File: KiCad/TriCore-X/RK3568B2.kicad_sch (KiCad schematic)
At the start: 1 part, among them U1 RK3568B2

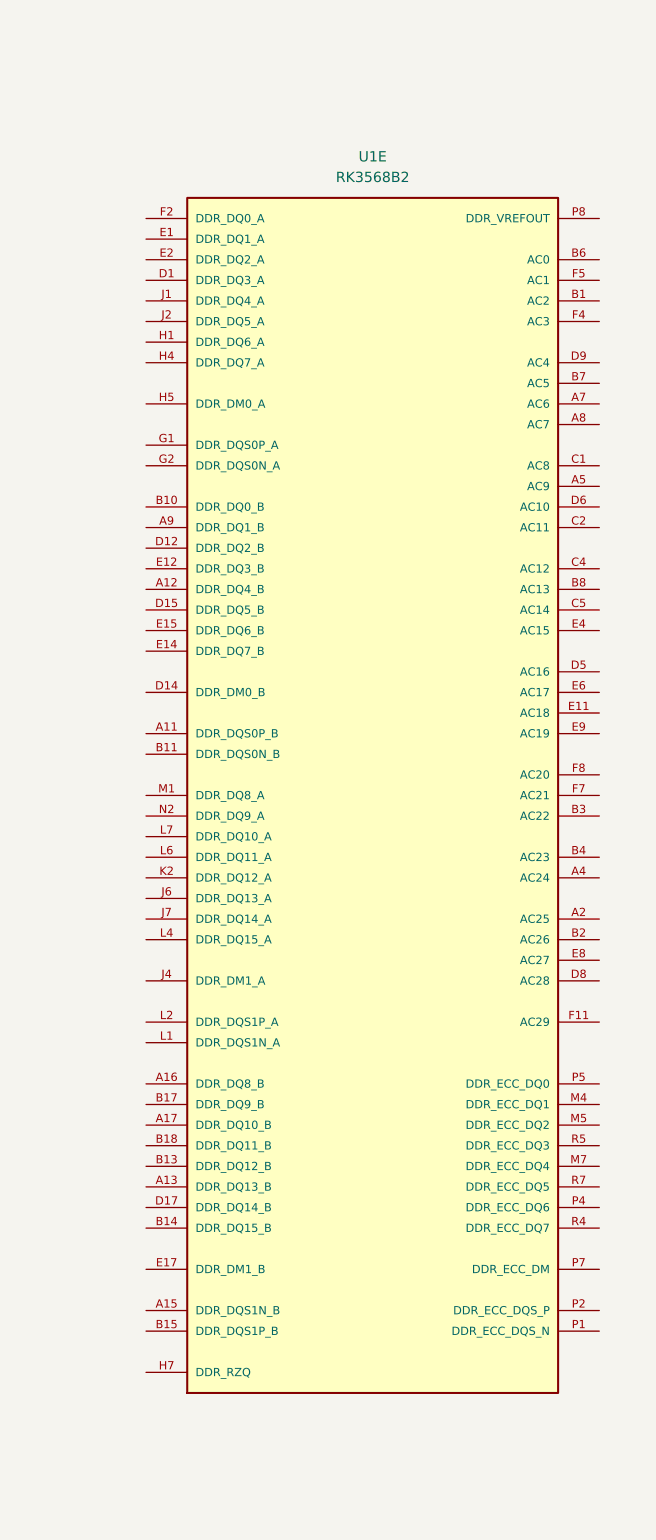
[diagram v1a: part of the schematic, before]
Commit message: feat : add some Expansion Ports (work in progress)
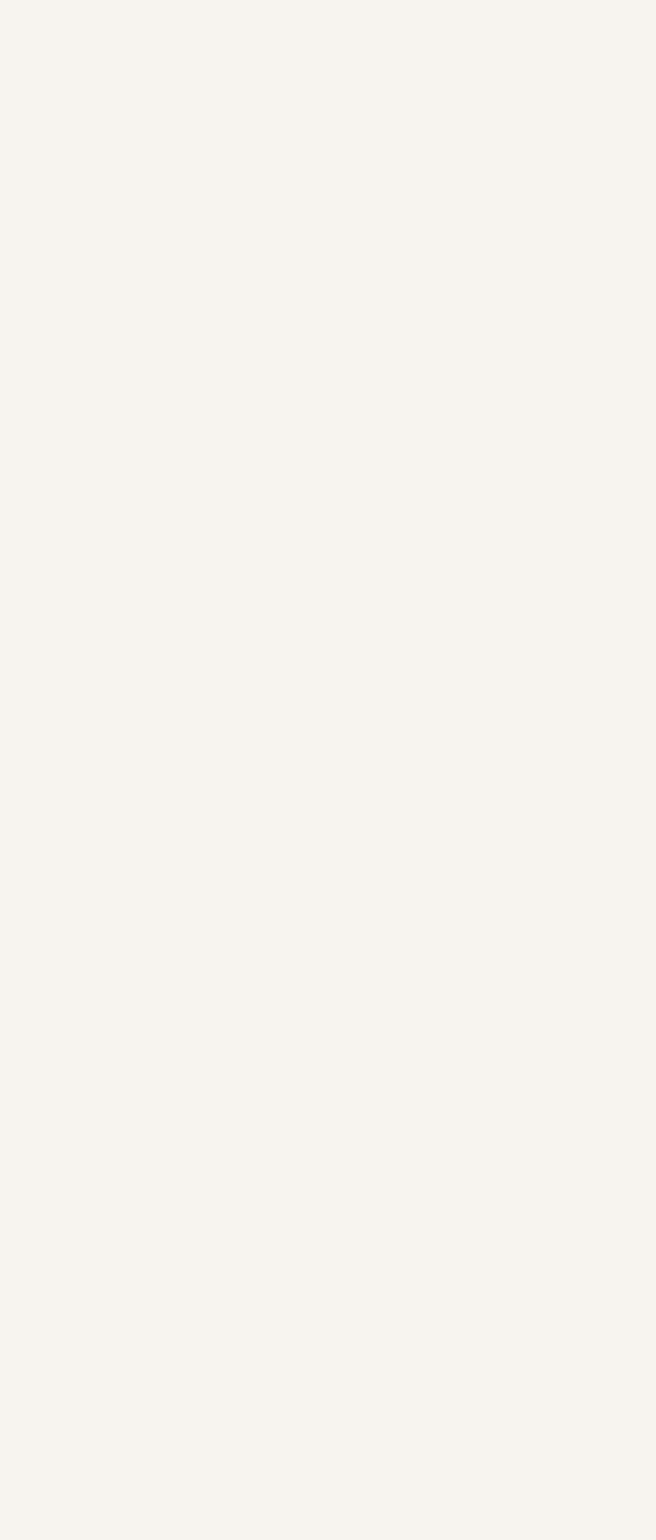
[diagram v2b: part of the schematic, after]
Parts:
- removed unit 5 of U1

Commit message: refactor: change core MCU to STM32H723 and add LPDDR4/HDMI support
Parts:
- removed unit 16 of U1
- added WIFI1: BL-M8822CU3-A, BL-M8822CU3-A:WIRELM-SMD_BL-M8822CU3-A, symbol BL-M8822CU3-A:BL-M8822CU3-A
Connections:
- net AVSS1: now also WIFI1.11 (GND), WIFI1.13 (GND), WIFI1.18 (GND), WIFI1.20 (GND), WIFI1.21 (GND), WIFI1.23 (GND), WIFI1.24 (GND), WIFI1.25 (GND), WIFI1.29 (GND), WIFI1.32 (GND), WIFI1.5 (GND), WIFI1.8 (GND)
- no-connect marks 0 -> 6

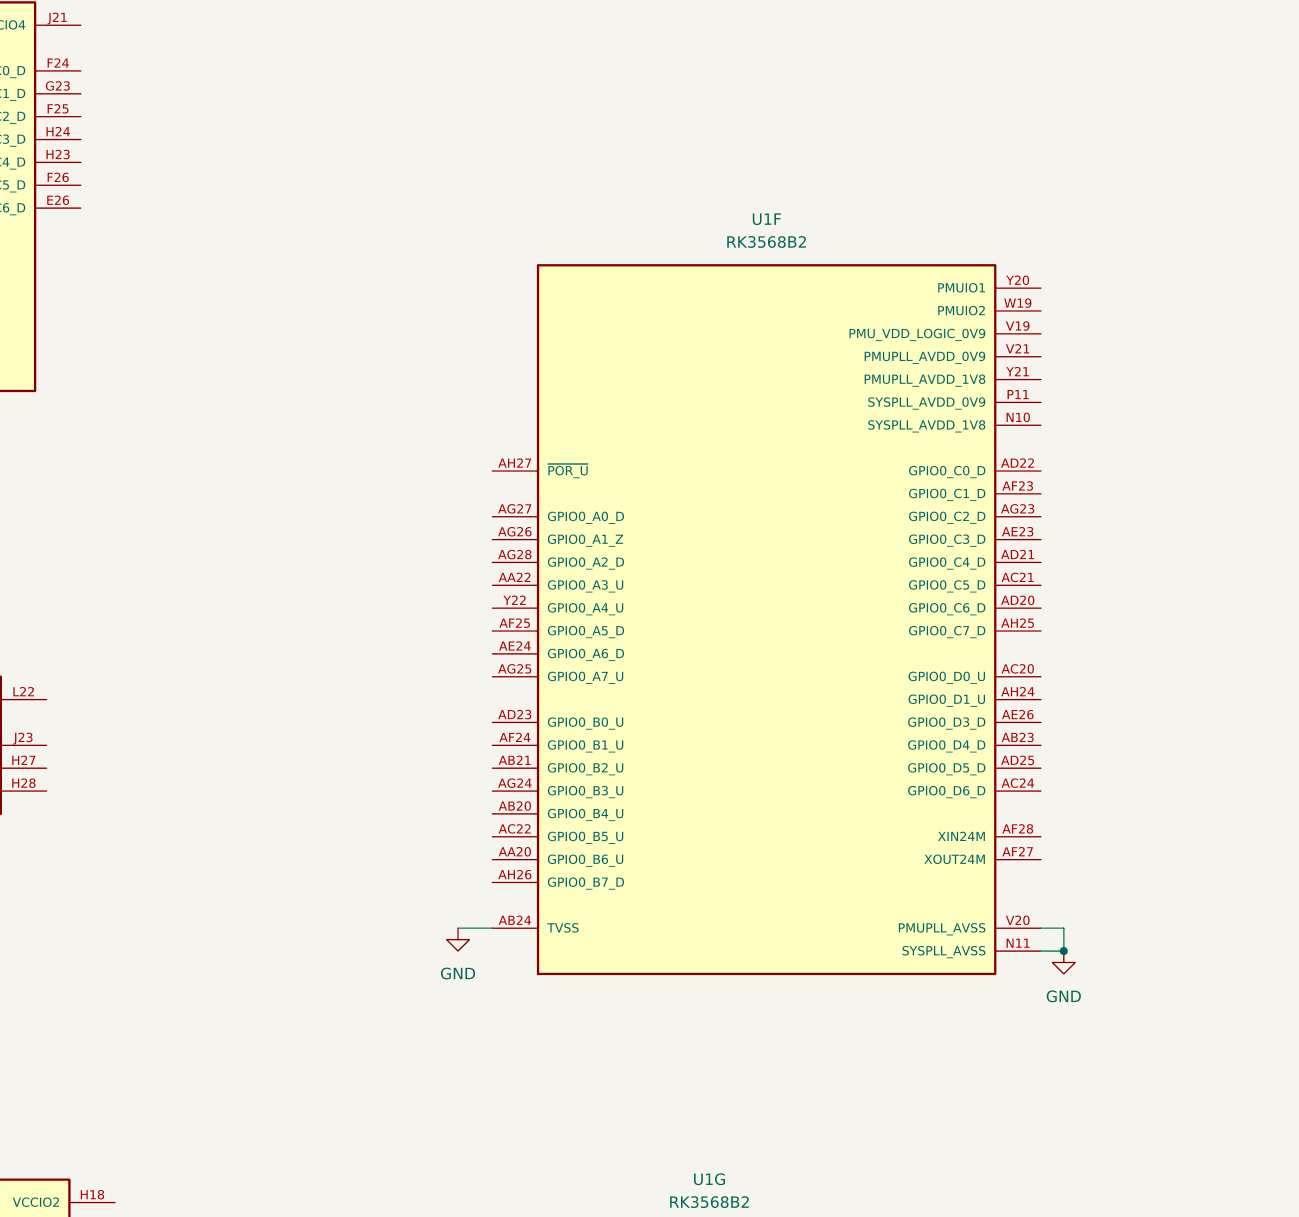
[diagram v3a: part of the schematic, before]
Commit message: feat: complete schematic for RK809-5 PMIC peripheral circuits
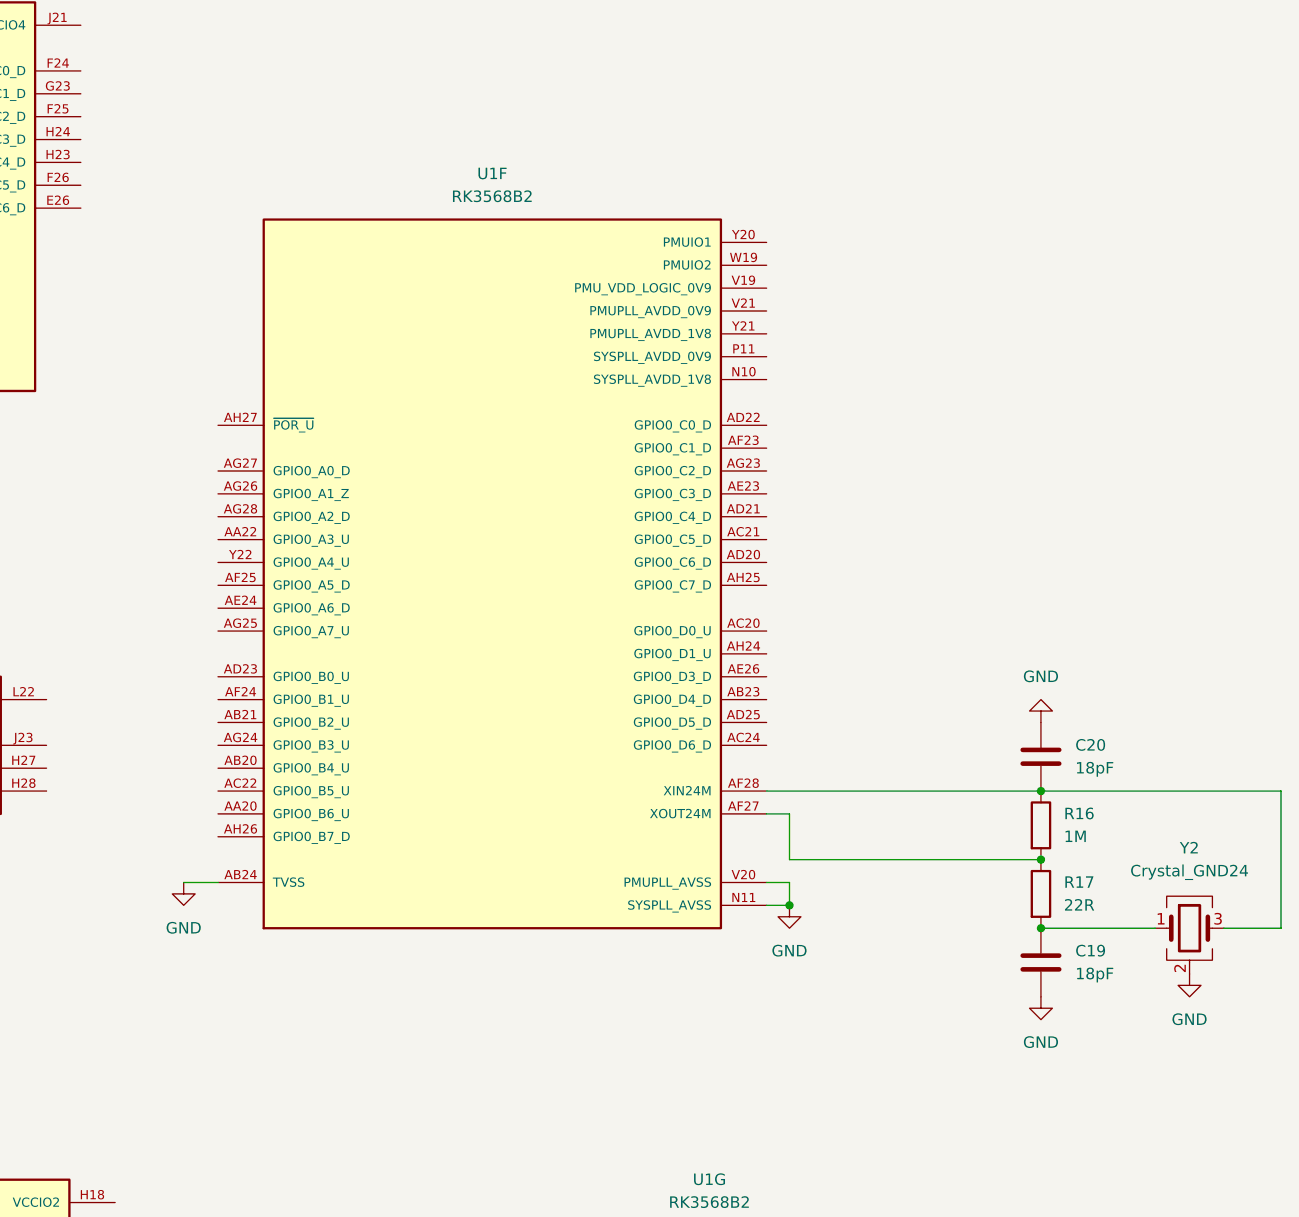
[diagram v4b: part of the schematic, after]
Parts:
- added C19, C20: 18pF, Capacitor_SMD:C_0402_1005Metric, symbol Device:C
- added R16: 1M, Resistor_SMD:R_0402_1005Metric, symbol Device:R
- added R17: 22R, Resistor_SMD:R_0402_1005Metric, symbol Device:R
- added Y2: Crystal_GND24, Crystal:Crystal_SMD_3225-4Pin_3.2x2.5mm, symbol Device:Crystal_GND24
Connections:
- net AVSS1: now also C19.2, C20.1, Y2.2 (G), Y2.4 (G)
- net at U1.AF27 (XOUT24M): now also R16.2, R17.1
- net at U1.AF28 (XIN24M): now also C20.2, R16.1, Y2.3
- new net: C19.1, R17.2, Y2.1
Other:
- moved on the sheet: U1F

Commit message: refactor: update schematic components and library references, including STM32H743 and new power symbols
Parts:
- removed C19, C20: 18pF, Capacitor_SMD:C_0402_1005Metric, symbol Device:C
- removed R16: 1M, Resistor_SMD:R_0402_1005Metric, symbol Device:R
- removed R17: 22R, Resistor_SMD:R_0402_1005Metric, symbol Device:R
- removed U1: RK3568B2, RK3568B2:BGA636C65P28X28_1900X1900X111, symbol RK3568B2:RK3568B2
- removed Y2: Crystal_GND24, Crystal:Crystal_SMD_3225-4Pin_3.2x2.5mm, symbol Device:Crystal_GND24
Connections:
- net AVSS1 renamed GND
